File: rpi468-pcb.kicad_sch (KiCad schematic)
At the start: 12 parts

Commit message: updates
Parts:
- removed C?: 22uF (solid tantalum), symbol Device:C
- removed J?: Conn_01x04_Female, symbol Connector:Conn_01x04_Female
- removed R?: 1k, symbol Device:R
- removed R?: 1.5k, symbol Device:R
- removed U?: AMS1117-3.3, Package_TO_SOT_SMD:SOT-223-3_TabPin2, symbol Regulator_Linear:AMS1117-3.3
- added J?: USB_A, symbol Connector:USB_A
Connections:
- net +3V3 is gone; now on net +5V: S?.10 (VDD)
- net +5V: now also J?.1 (VBUS)
- net GND: now also J?.4 (GND), J?.5 (Shield)
- net at S?.8 (HSD1-): now also J?.2 (D-)
- net at S?.2 (HSD1+): now also J?.3 (D+)

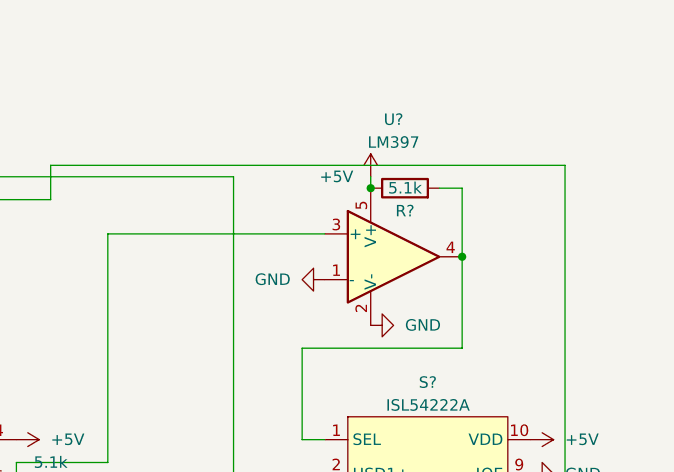
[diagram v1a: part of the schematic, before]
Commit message: added breakout boardk
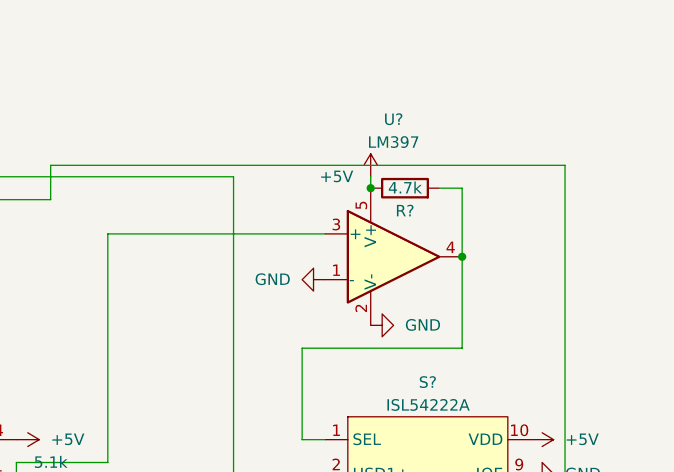
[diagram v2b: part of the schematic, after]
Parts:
- R?: value 5.1k -> 4.7k
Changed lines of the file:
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@@
     (in_bom yes) (on_board yes)
     (property "Reference" "R?" (id 0) (at 143.51 55.88 90))
-    (property "Value" "5.1k" (id 1) (at 143.51 53.34 90))
+    (property "Value" "4.7k" (id 1) (at 143.51 53.34 90))
     (property "Footprint" "" (id 2) (at 143.51 55.118 90)
       (effects (font (size 1.27 1.27)) hide)
@@
     )
     (path "/38762778-9a44-491f-be9d-282c618545cb"
-      (reference "R?") (unit 1) (value "5.1k") (footprint "")
+      (reference "R?") (unit 1) (value "4.7k") (footprint "")
     )
     (path "/f619ccc9-65b6-46d1-9876-505c58d8035a"

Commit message: updates
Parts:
- removed S?: ISL54222A, symbol library:ISL54222A
- added R? (x3): R, symbol Device:R
- added S?: ISL54225, symbol library:ISL54225
- R?: value 4.7k -> 5.1k
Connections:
- net +5V: now also R?.1, S?.10 (VDD)
- net GND: now also R?.2, S?.11 (THERM), S?.5 (GND), S?.9 (!OE); no longer U?.1 (-)
- net at R?.2, U?.4: now also R?.2, S?.1 (SEL)
- net at J?.2 (D-): now also S?.8 (HSD1-)
- net at J?.3 (D+): now also S?.2 (HSD1+)
- net at J?.A6 (D+), J?.B6 (D+): now also S?.3 (HSD2+)
- net at J?.3 (Pin_3): now also S?.4 (D+)
- net at J?.2 (Pin_2): now also S?.6 (D-)
- net at J?.A7 (D-), J?.B7 (D-): now also S?.7 (HSD2-)
- net at J?.A5 (CC1), R?.1: now also U?.1 (-); no longer U?.3 (+)
- new net: R?.1, R?.1, R?.2, U?.3 (+)
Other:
- moved on the sheet: R?, U?

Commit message: updates
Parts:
- R?: value R -> 1k; footprint (none) -> Resistor_SMD:R_0805_2012Metric
- R? (x3): footprint (none) -> Resistor_SMD:R_0805_2012Metric
- R?: value R -> 100k; footprint (none) -> Resistor_SMD:R_0805_2012Metric
- R?: value R -> 50k; footprint (none) -> Resistor_SMD:R_0805_2012Metric
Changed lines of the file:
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@@
   )
   (symbol (lib_id "Device:R") (at 193.04 104.14 0) (unit 1)
-    (in_bom yes) (on_board yes) (fields_autoplaced)
-    (property "Reference" "R?" (id 0) (at 195.58 102.8699 0)
-      (effects (font (size 1.27 1.27)) (justify left))
-    )
-    (property "Value" "R" (id 1) (at 195.58 105.4099 0)
-      (effects (font (size 1.27 1.27)) (justify left))
-    )
-    (property "Footprint" "" (id 2) (at 191.262 104.14 90)
+    (in_bom yes) (on_board yes)
+    (property "Reference" "R?" (id 0) (at 189.23 104.14 0)
+      (effects (font (size 1.27 1.27)) (justify left))
+    )
+    (property "Value" "1k" (id 1) (at 194.31 104.14 0)
+      (effects (font (size 1.27 1.27)) (justify left))
+    )
+    (property "Footprint" "Resistor_SMD:R_0805_2012Metric" (id 2) (at 191.262 104.14 90)
       (effects (font (size 1.27 1.27)) hide)
     )
@@
     (property "Reference" "R?" (id 0) (at 104.14 88.9 90))
     (property "Value" "5.1k" (id 1) (at 104.14 91.44 90))
-    (property "Footprint" "" (id 2) (at 104.14 90.678 90)
+    (property "Footprint" "Resistor_SMD:R_0805_2012Metric" (id 2) (at 104.14 90.678 90)
       (effects (font (size 1.27 1.27)) hide)
     )
@@
     (in_bom yes) (on_board yes)
     (property "Reference" "R?" (id 0) (at 214.63 77.47 90))
-    (property "Value" "5.1k" (id 1) (at 214.63 80.01 90))
-    (property "Footprint" "" (id 2) (at 214.63 81.788 90)
+    (property "Value" "5.1k" (id 1) (at 214.63 82.55 90))
+    (property "Footprint" "Resistor_SMD:R_0805_2012Metric" (id 2) (at 214.63 81.788 90)
       (effects (font (size 1.27 1.27)) hide)
     )
@@
   )
   (symbol (lib_id "Device:R") (at 193.04 86.36 0) (unit 1)
-    (in_bom yes) (on_board yes) (fields_autoplaced)
-    (property "Reference" "R?" (id 0) (at 195.58 85.0899 0)
-      (effects (font (size 1.27 1.27)) (justify left))
-    )
-    (property "Value" "R" (id 1) (at 195.58 87.6299 0)
-      (effects (font (size 1.27 1.27)) (justify left))
-    )
-    (property "Footprint" "" (id 2) (at 191.262 86.36 90)
+    (in_bom yes) (on_board yes)
+    (property "Reference" "R?" (id 0) (at 189.23 86.36 0)
+      (effects (font (size 1.27 1.27)) (justify left))
+    )
+    (property "Value" "100k" (id 1) (at 194.31 86.36 0)
+      (effects (font (size 1.27 1.27)) (justify left))
+    )
+    (property "Footprint" "Resistor_SMD:R_0805_2012Metric" (id 2) (at 191.262 86.36 90)
       (effects (font (size 1.27 1.27)) hide)
     )
@@
   (symbol (lib_id "Device:R") (at 209.55 100.33 90) (unit 1)
     (in_bom yes) (on_board yes)
-    (property "Reference" "R?" (id 0) (at 208.28 102.87 90))
-    (property "Value" "R" (id 1) (at 210.82 102.87 90))
-    (property "Footprint" "" (id 2) (at 209.55 102.108 90)
+    (property "Reference" "R?" (id 0) (at 209.55 97.79 90))
+    (property "Value" "50k" (id 1) (at 209.55 102.87 90))
+    (property "Footprint" "Resistor_SMD:R_0805_2012Metric" (id 2) (at 209.55 102.108 90)
       (effects (font (size 1.27 1.27)) hide)
     )
@@
     (property "Reference" "R?" (id 0) (at 104.14 86.36 90))
     (property "Value" "5.1k" (id 1) (at 104.14 83.82 90))
-    (property "Footprint" "" (id 2) (at 104.14 88.138 90)
+    (property "Footprint" "Resistor_SMD:R_0805_2012Metric" (id 2) (at 104.14 88.138 90)
       (effects (font (size 1.27 1.27)) hide)
     )
@@
   (symbol (lib_id "Comparator:LM397") (at 212.09 87.63 0) (unit 1)
     (in_bom yes) (on_board yes)
-    (property "Reference" "U?" (id 0) (at 212.09 72.39 0))
-    (property "Value" "LM397" (id 1) (at 212.09 74.93 0))
+    (property "Reference" "U?" (id 0) (at 212.09 71.12 0))
+    (property "Value" "LM397" (id 1) (at 212.09 73.66 0))
     (property "Footprint" "Package_TO_SOT_SMD:SOT-23-5" (id 2) (at 213.36 102.87 0)
       (effects (font (size 1.27 1.27)) hide)
@@
     )
     (path "/1829c383-9c86-4d52-a146-f19816fab1a7"
-      (reference "R?") (unit 1) (value "R") (footprint "")
+      (reference "R?") (unit 1) (value "1k") (footprint "Resistor_SMD:R_0805_2012Metric")
     )
     (path "/2fa03c2b-51fc-4456-bdb0-f263cbb97ec2"
-      (reference "R?") (unit 1) (value "5.1k") (footprint "")
+      (reference "R?") (unit 1) (value "5.1k") (footprint "Resistor_SMD:R_0805_2012Metric")
     )
     (path "/38762778-9a44-491f-be9d-282c618545cb"
-      (reference "R?") (unit 1) (value "5.1k") (footprint "")
+      (reference "R?") (unit 1) (value "5.1k") (footprint "Resistor_SMD:R_0805_2012Metric")
     )
     (path "/6da03d20-475c-43ba-9c2d-1d8574e4fab1"
-      (reference "R?") (unit 1) (value "R") (footprint "")
+      (reference "R?") (unit 1) (value "100k") (footprint "Resistor_SMD:R_0805_2012Metric")
     )
     (path "/de324e25-0d21-4c49-8736-7d79013e10c4"
-      (reference "R?") (unit 1) (value "R") (footprint "")
+      (reference "R?") (unit 1) (value "50k") (footprint "Resistor_SMD:R_0805_2012Metric")
     )
     (path "/f619ccc9-65b6-46d1-9876-505c58d8035a"
-      (reference "R?") (unit 1) (value "5.1k") (footprint "")
+      (reference "R?") (unit 1) (value "5.1k") (footprint "Resistor_SMD:R_0805_2012Metric")
     )
     (path "/0509dcab-bdbc-491a-8667-3da45ae2b029"

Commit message: started layout
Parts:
- J1: renamed from J?; footprint (none) -> Connector_USB:USB_A_Molex_67643_Horizontal
- J2: renamed from J?; footprint (none) -> Connector_USB:USB_C_Receptacle_Amphenol_12401548E4-2A
- J3: renamed from J?; footprint (none) -> Connector_Wuerth:Wuerth_WR-WTB_64800411622_1x04_P1.50mm_Vertical
- S1: renamed from S?; footprint (none) -> Package_DFN_QFN:TDFN-10-1EP_2x3mm_P0.5mm_EP0.9x2mm_ThermalVias
- gave numbers to parts that had none: 7

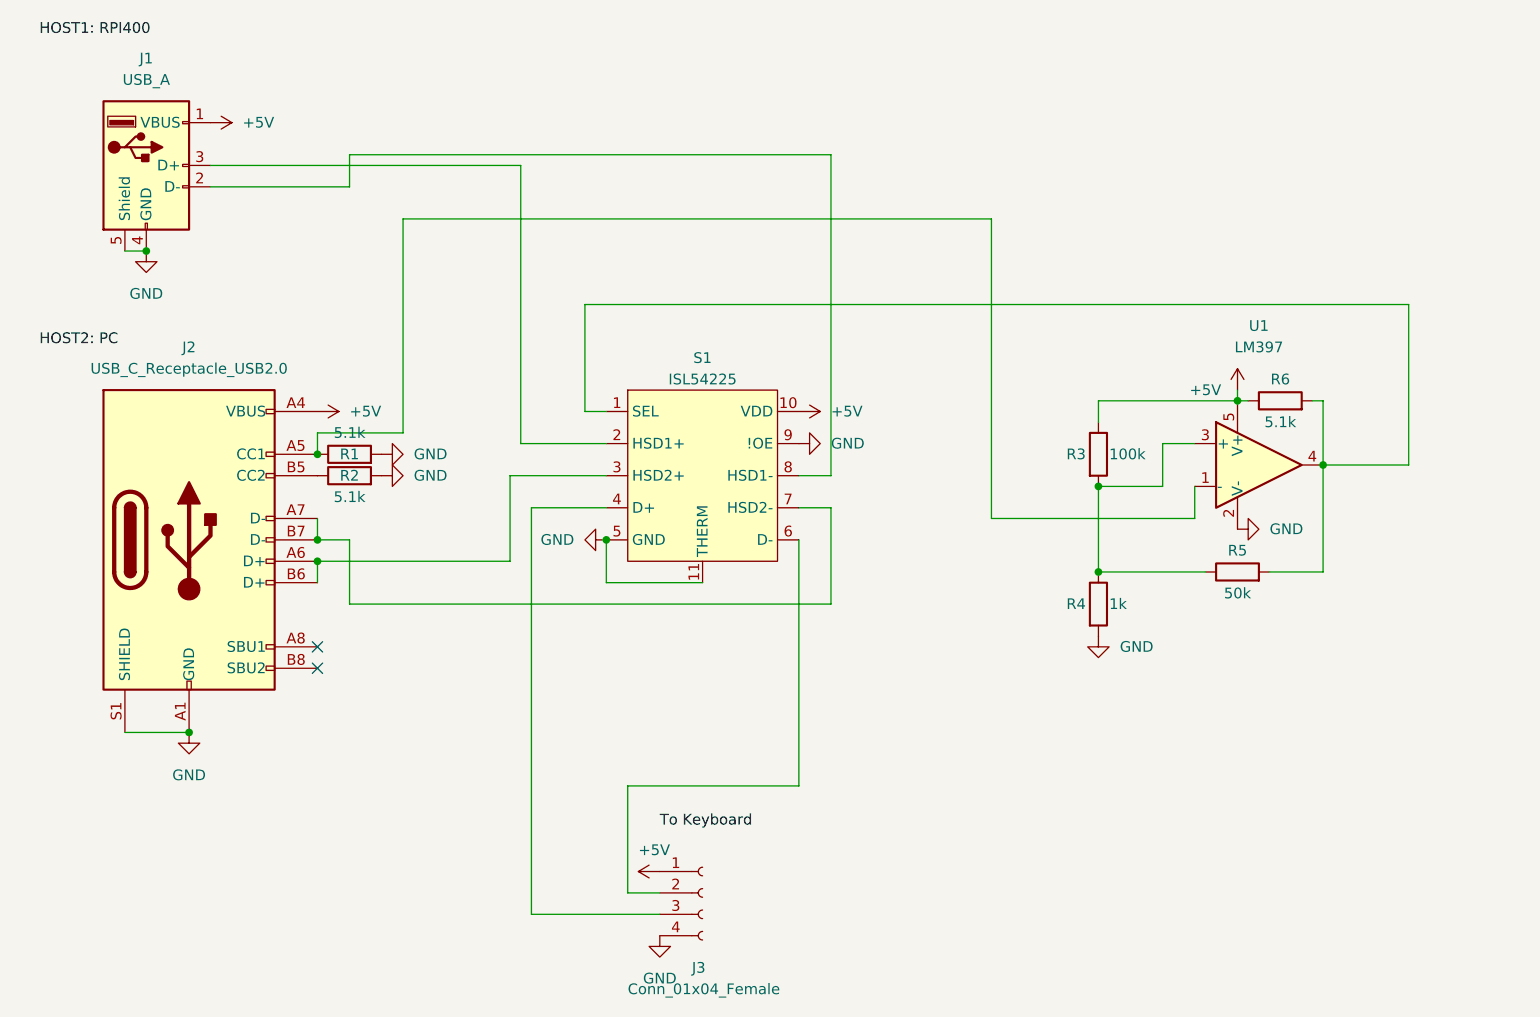
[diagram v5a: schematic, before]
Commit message: fixed bug, schematic works for breadboard
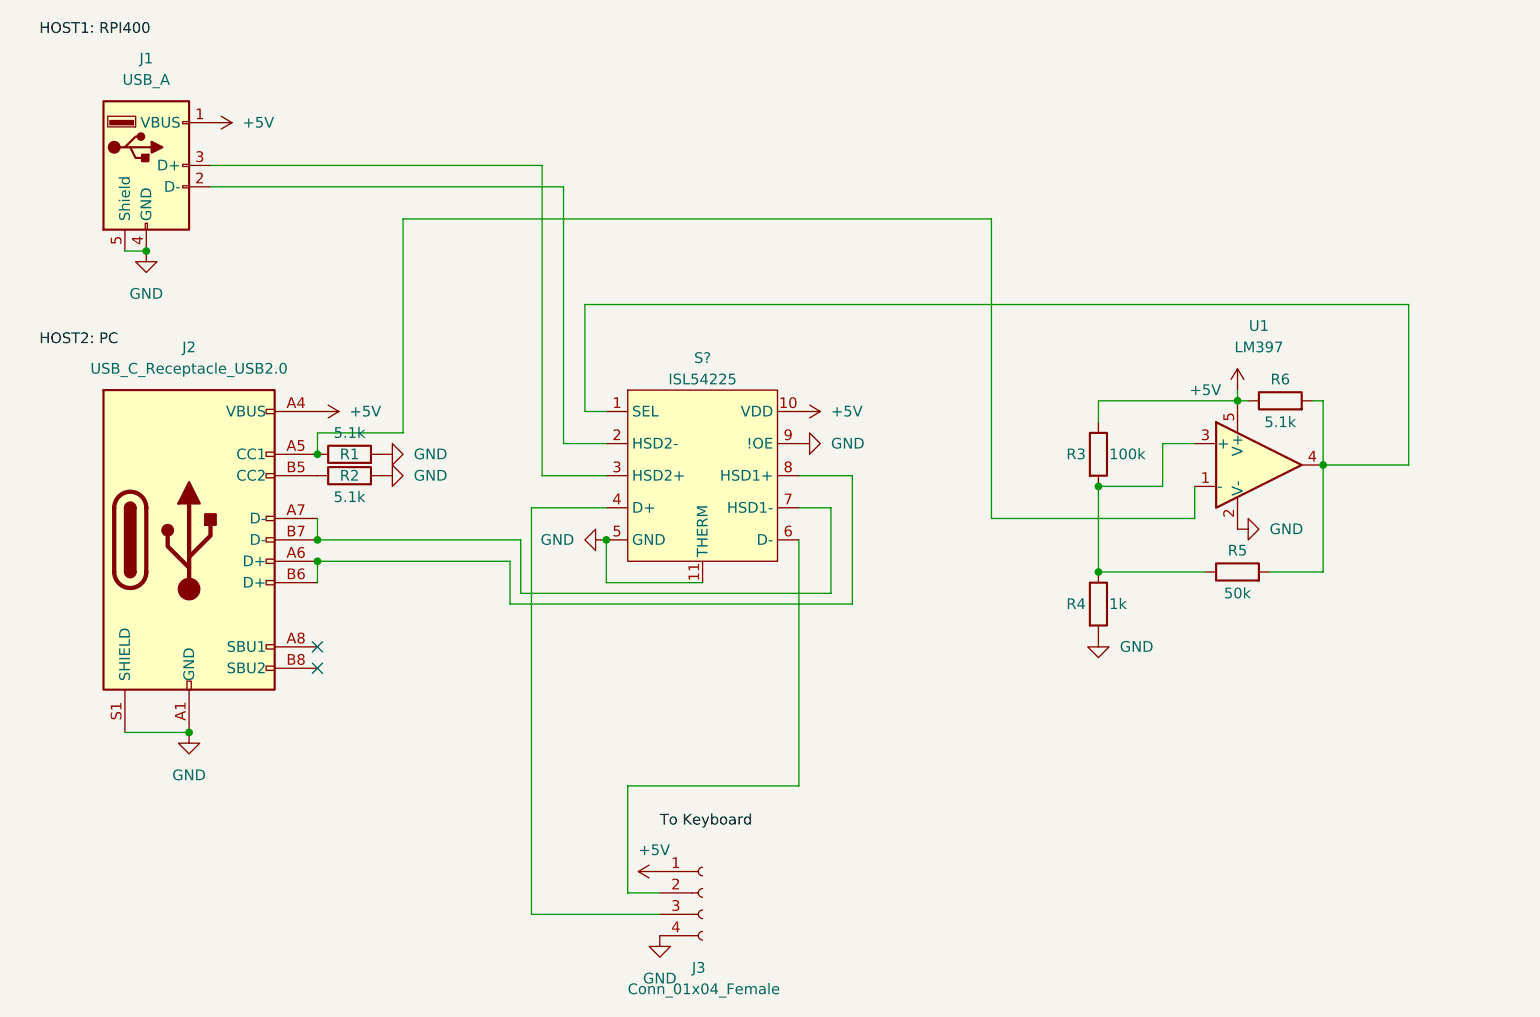
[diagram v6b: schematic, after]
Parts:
- removed S1: ISL54225, Package_DFN_QFN:TDFN-10-1EP_2x3mm_P0.5mm_EP0.9x2mm_ThermalVias, symbol library:ISL54225
- added S?: ISL54225, symbol library:ISL54225
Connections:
- net +5V: now also S?.10 (VDD)
- net GND: now also S?.11 (THERM), S?.5 (GND), S?.9 (!OE)
- net at R5.2, R6.2, U1.4: now also S?.1 (SEL)
- net at J1.3 (D+): now also S?.3 (HSD2+)
- net at J2.A6 (D+), J2.B6 (D+): now also S?.8 (HSD1+)
- net at J3.3 (Pin_3): now also S?.4 (D+)
- net at J3.2 (Pin_2): now also S?.6 (D-)
- net at J2.A7 (D-), J2.B7 (D-): now also S?.7 (HSD1-)
- net at J1.2 (D-): now also S?.2 (HSD2-)
